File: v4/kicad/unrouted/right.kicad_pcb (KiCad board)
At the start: 2 copper layers, 160 x 118.6 mm, 72 parts

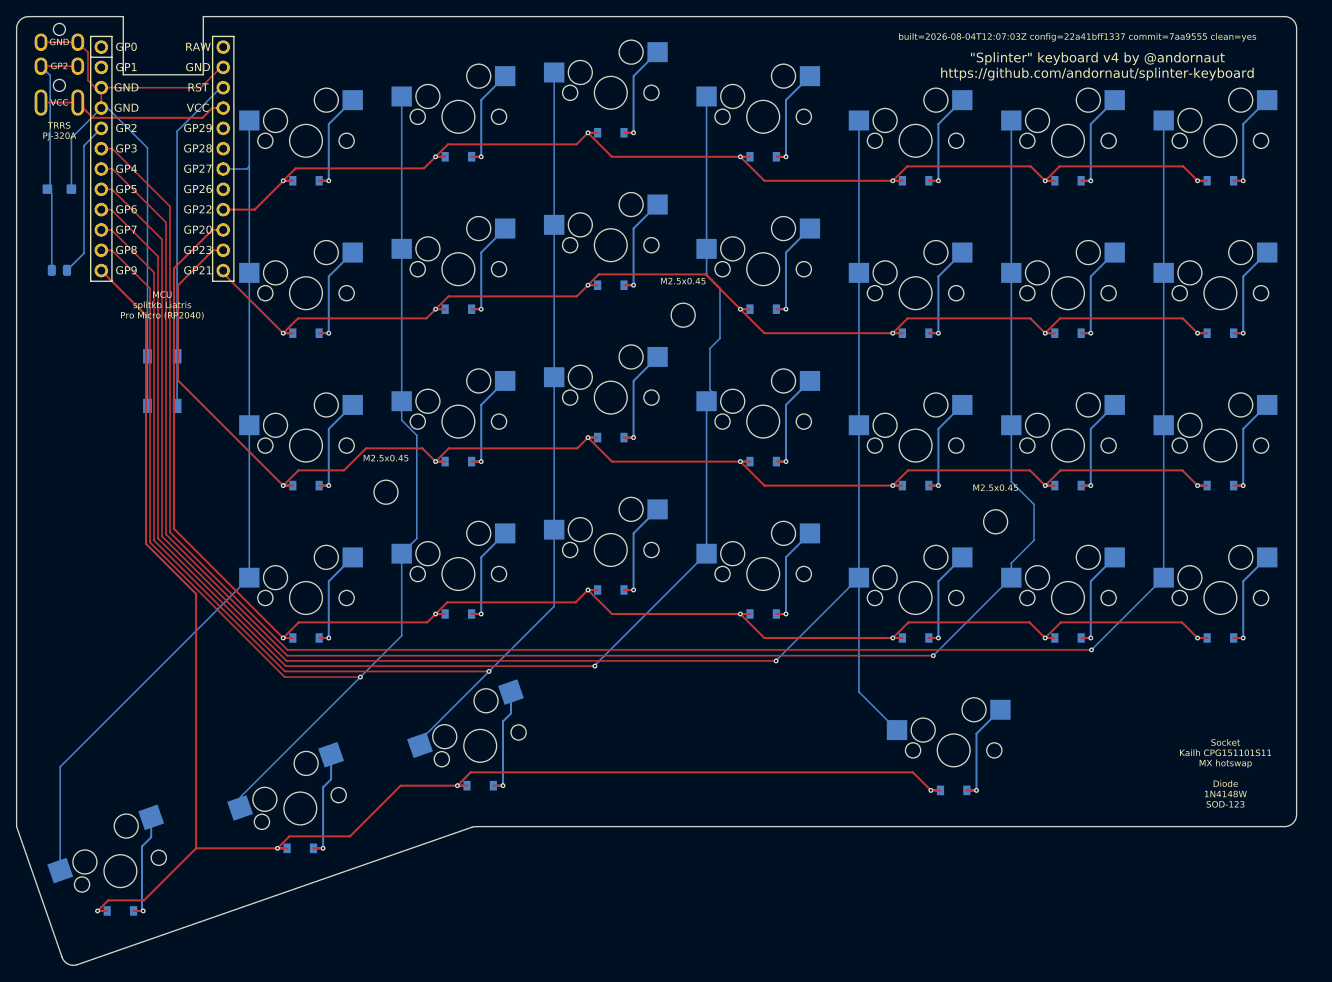
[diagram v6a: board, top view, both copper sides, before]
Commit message: v4: re-route the TRRS data segment on both halves
Re-runs DATA_RAW (TRRS ring 2 to the TVS and the series resistor) on
B.Cu on both halves, and nudges the mirror_five_mod, mirror_four_mod and
MCU GND jogs on the right. DATA_RAW grows 30.99 to 31.98mm (left) and
29.69 to 30.96mm (right); every other net is untouched.

Track count 324 to 327 (left) and 334 to 340 (right), vias 36/38,
teardrops 281/297 and 0 unconnected, all unchanged.
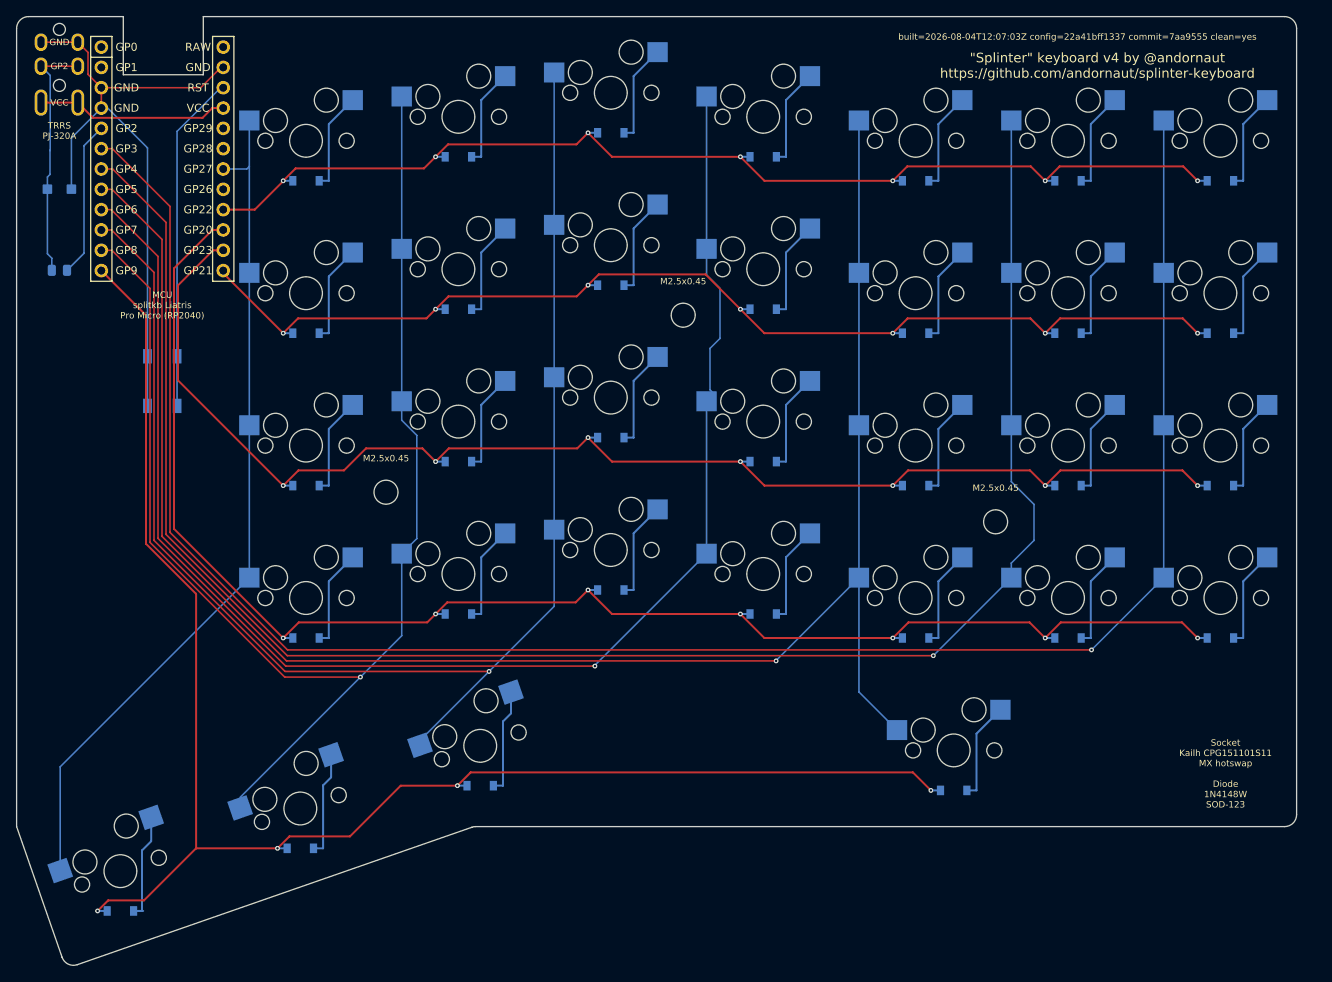
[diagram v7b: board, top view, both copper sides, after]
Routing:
- net P15: track 148.1 -> 139.7 mm
- net P16: track 178.5 -> 170.1 mm
- net P14: track 199.3 -> 190.9 mm
- net P10: track 150.9 -> 142.5 mm
- net P9: track 199.0 -> 194.2 mm
- net DATA_RAW: track 29.7 -> 31.0 mm
- net dash_upper: track 13.7 -> 12.5 mm, vias 1 -> 0
- net dash_num: track 13.7 -> 12.5 mm, vias 1 -> 0
- net dash_lower: track 13.7 -> 12.5 mm, vias 1 -> 0
- net dash_home: track 13.7 -> 12.5 mm, vias 1 -> 0
- net zero_upper: track 13.7 -> 12.5 mm, vias 1 -> 0
- net zero_num: track 13.7 -> 12.5 mm, vias 1 -> 0
- net zero_lower: track 13.7 -> 12.5 mm, vias 1 -> 0
- net zero_home: track 13.7 -> 12.5 mm, vias 1 -> 0
- net mirror_three_mod: track 14.5 -> 13.3 mm, vias 1 -> 0
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
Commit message: v4: rebuild the boards from a clean tree
Re-stamps all four boards with clean=yes commit=1db0e07. Copper is
unchanged.
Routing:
- net P15: track 139.7 -> 148.1 mm
- net P14: track 190.9 -> 199.3 mm
- net P16: track 170.1 -> 178.5 mm
- net P10: track 142.5 -> 150.9 mm
- net P9: track 194.2 -> 199.0 mm
- net dash_upper: track 12.5 -> 13.7 mm, vias 0 -> 1
- net dash_num: track 12.5 -> 13.7 mm, vias 0 -> 1
- net dash_lower: track 12.5 -> 13.7 mm, vias 0 -> 1
- net dash_home: track 12.5 -> 13.7 mm, vias 0 -> 1
- net zero_upper: track 12.5 -> 13.7 mm, vias 0 -> 1
- net zero_num: track 12.5 -> 13.7 mm, vias 0 -> 1
- net zero_lower: track 12.5 -> 13.7 mm, vias 0 -> 1
- net zero_home: track 12.5 -> 13.7 mm, vias 0 -> 1
- net mirror_three_mod: track 13.3 -> 14.5 mm, vias 0 -> 1
- net mirror_four_upper: track 12.5 -> 13.7 mm, vias 0 -> 1
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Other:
- board text added: "built=2026-08-04T12:23:37Z config=22a41bff1337 commit=1db0e07 clean=yes"
- board text removed: "built=2026-08-04T12:07:03Z config=22a41bff1337 commit=7aa9555 clean=yes"
